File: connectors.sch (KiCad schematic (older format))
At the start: 3 parts, among them P1 CONN_02X04, P3 CONN_02X04

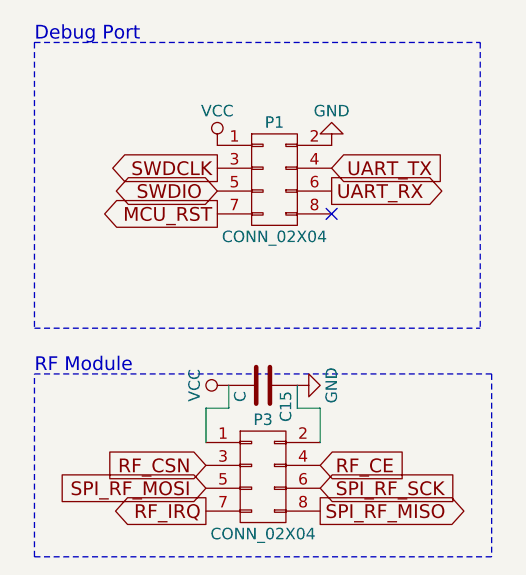
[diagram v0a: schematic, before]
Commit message: Fix Boot0 pin and add prices per component
Signed-off-by: Philip Luyckx <philip.luyckx@gmail.com>
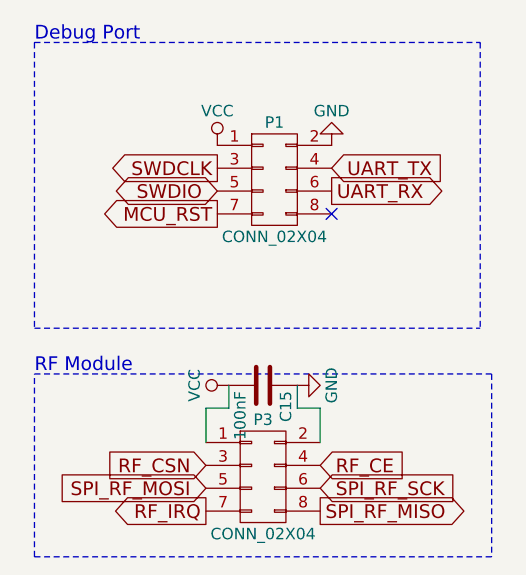
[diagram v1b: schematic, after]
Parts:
- C15: value C -> 100nF; Price (none) -> 0.02
- P1: Price (none) -> 0.13
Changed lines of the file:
@@
 F 2 "Socket_Strips:Socket_Strip_Straight_2x04" H 3150 2850 50  0001 C CNN
 F 3 "" H 3150 2850 50  0000 C CNN
+F 4 "0.13" H 3150 4050 60  0001 C CNN "Price"
 	1    3150 4050
 	1    0    0    -1
@@
 P 3100 4950
 F 0 "C15" H 3125 5050 50  0000 L CNN
-F 1 "C" H 3125 4850 50  0000 L CNN
+F 1 "100nF" H 3125 4850 50  0000 L CNN
 F 2 "Resistors_SMD:R_0805" H 3138 4800 50  0001 C CNN
 F 3 "" H 3100 4950 50  0000 C CNN
+F 4 "0.02" H 3100 4950 60  0001 C CNN "Price"
 	1    3100 4950
 	0    1    1    0

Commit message: Update schematics for V3:
 * Change DHT22 to HTU21D
 * Change schematic for MCP6044
 * Correct unused opamp + power supply
 * Reassign some cpu pins (for HTU21D)
 * Add LDO power supply for 1.8V
 * Update STM32CubeMx project
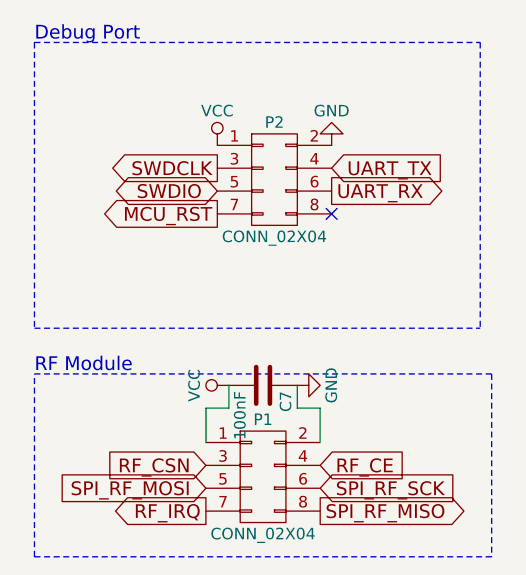
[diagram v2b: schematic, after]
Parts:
- renumbered C15 to C7, P3 to P1, P1 to P2
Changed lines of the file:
@@
 LIBS:CustomModules
 LIBS:CustomPower
-LIBS:CustomPowerConvertors
 LIBS:CustomTransistors
 LIBS:Custom_ShiftRegisters
@@
 LIBS:Relais
 LIBS:CustomDevices
+LIBS:CustomPowerConvertors
 LIBS:Sensor-cache
 EELAYER 25 0
@@
 $EndDescr
 $Comp
-L VCC #PWR012
+L VCC #PWR14
 U 1 1 565F5F2C
 P 2900 3900
-F 0 "#PWR012" H 2900 3750 50  0001 C CNN
+F 0 "#PWR14" H 2900 3750 50  0001 C CNN
 F 1 "VCC" H 2900 4050 50  0000 C CNN
 F 2 "" H 2900 3900 60  0000 C CNN
@@
 UART_TX
 $Comp
-L CONN_02X04 P3
+L CONN_02X04 P1
 U 1 1 56622904
 P 3100 5350
-F 0 "P3" H 3100 5600 50  0000 C CNN
+F 0 "P1" H 3100 5600 50  0000 C CNN
 F 1 "CONN_02X04" H 3100 5100 50  0000 C CNN
 F 2 "Socket_Strips:Socket_Strip_Straight_2x04" H 3100 4150 60  0001 C CNN
@@
 $EndComp
 $Comp
-L VCC #PWR013
+L VCC #PWR15
 U 1 1 56622A6F
 P 2950 4950
-F 0 "#PWR013" H 2950 4800 50  0001 C CNN
+F 0 "#PWR15" H 2950 4800 50  0001 C CNN
 F 1 "VCC" H 2950 5100 50  0000 C CNN
 F 2 "" H 2950 4950 60  0000 C CNN
@@
 $EndComp
 $Comp
-L GND #PWR014
+L GND #PWR16
 U 1 1 56622A8F
 P 3250 4950
-F 0 "#PWR014" H 3250 4700 50  0001 C CNN
+F 0 "#PWR16" H 3250 4700 50  0001 C CNN
 F 1 "GND" H 3250 4800 50  0000 C CNN
 F 2 "" H 3250 4950 60  0000 C CNN
@@
 	2100 4700 4050 4700
 $Comp
-L GND #PWR015
+L GND #PWR17
 U 1 1 5669F0F1
 P 3400 3900
-F 0 "#PWR015" H 3400 3650 50  0001 C CNN
+F 0 "#PWR17" H 3400 3650 50  0001 C CNN
 F 1 "GND" H 3400 3750 50  0000 C CNN
 F 2 "" H 3400 3900 60  0000 C CNN
@@
 	2100 3450 2100 4700
 $Comp
-L CONN_02X04 P1
+L CONN_02X04 P2
 U 1 1 56DBFF1C
 P 3150 4050
-F 0 "P1" H 3150 4300 50  0000 C CNN
+F 0 "P2" H 3150 4300 50  0000 C CNN
 F 1 "CONN_02X04" H 3150 3800 50  0000 C CNN
 F 2 "Socket_Strips:Socket_Strip_Straight_2x04" H 3150 2850 50  0001 C CNN
@@
 $EndComp
 $Comp
-L C C15
+L C C7
 U 1 1 56DC195B
 P 3100 4950
-F 0 "C15" H 3125 5050 50  0000 L CNN
+F 0 "C7" H 3125 5050 50  0000 L CNN
 F 1 "100nF" H 3125 4850 50  0000 L CNN
 F 2 "Resistors_SMD:R_0805" H 3138 4800 50  0001 C CNN

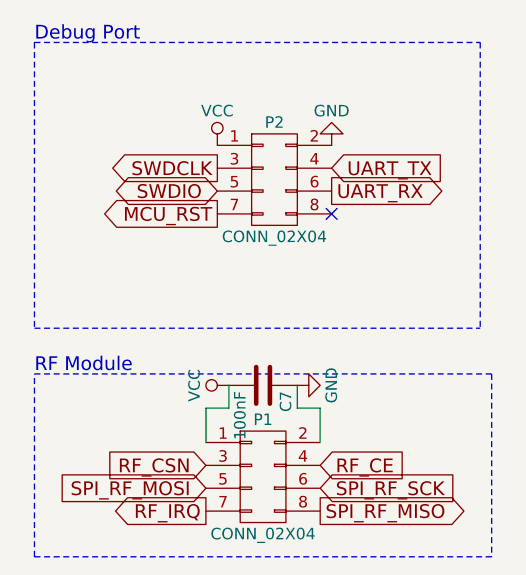
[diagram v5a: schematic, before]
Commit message: Update connectors to custom ones
Signed-off-by: Philip Luyckx <philip.luyckx@gmail.com>
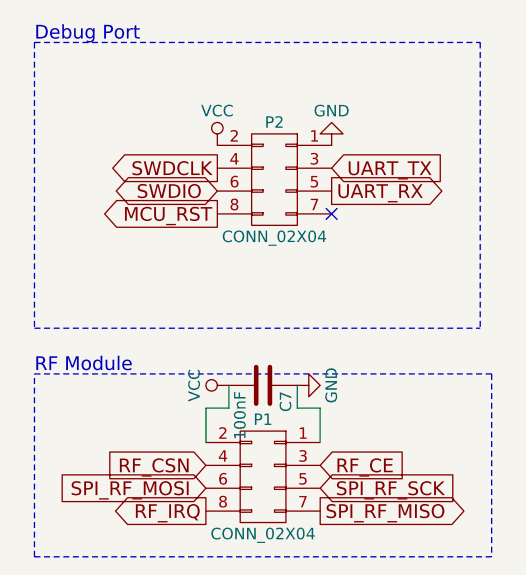
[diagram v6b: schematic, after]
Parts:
- P1: footprint Socket_Strips:Socket_Strip_Straight_2x04 -> PinHeaders:Pin_Header_Straight_2x04_SMD
- P2: footprint Socket_Strips:Socket_Strip_Straight_2x04 -> PinHeaders:Pin_Header_Straight_2x04_TH
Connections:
- net GND: now also P1.1 (P1), P2.1 (P1); no longer P1.2 (P2), P2.2 (P2)
- net MCU_RST: now also P2.8 (P8); no longer P2.7 (P7)
- net RF_CE: now also P1.3 (P3); no longer P1.4 (P4)
- net RF_CSN: now also P1.4 (P4); no longer P1.3 (P3)
- net RF_IRQ: now also P1.8 (P8); no longer P1.7 (P7)
- net SPI_RF_MISO: now also P1.7 (P7); no longer P1.8 (P8)
- net SPI_RF_MOSI: now also P1.6 (P6); no longer P1.5 (P5)
- net SPI_RF_SCK: now also P1.5 (P5); no longer P1.6 (P6)
- net SWDCLK: now also P2.4 (P4); no longer P2.3 (P3)
- net SWDIO: now also P2.6 (P6); no longer P2.5 (P5)
- net UART_RX: now also P2.5 (P5); no longer P2.6 (P6)
- net UART_TX: now also P2.3 (P3); no longer P2.4 (P4)
- net VCC: now also P1.2 (P2), P2.2 (P2); no longer P1.1 (P1), P2.1 (P1)
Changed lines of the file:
@@
 $EndDescr
 $Comp
-L VCC #PWR16
+L VCC #PWR016
 U 1 1 565F5F2C
 P 2900 3900
-F 0 "#PWR16" H 2900 3750 50  0001 C CNN
+F 0 "#PWR016" H 2900 3750 50  0001 C CNN
 F 1 "VCC" H 2900 4050 50  0000 C CNN
 F 2 "" H 2900 3900 60  0000 C CNN
@@
 F 0 "P1" H 3100 5600 50  0000 C CNN
 F 1 "CONN_02X04" H 3100 5100 50  0000 C CNN
-F 2 "Socket_Strips:Socket_Strip_Straight_2x04" H 3100 4150 60  0001 C CNN
+F 2 "PinHeaders:Pin_Header_Straight_2x04_SMD" H 3100 4150 60  0001 C CNN
 F 3 "" H 3100 4150 60  0000 C CNN
 	1    3100 5350
-	1    0    0    -1
+	-1   0    0    -1
 $EndComp
 $Comp
-L VCC #PWR17
+L VCC #PWR017
 U 1 1 56622A6F
 P 2950 4950
-F 0 "#PWR17" H 2950 4800 50  0001 C CNN
+F 0 "#PWR017" H 2950 4800 50  0001 C CNN
 F 1 "VCC" H 2950 5100 50  0000 C CNN
 F 2 "" H 2950 4950 60  0000 C CNN
@@
 $EndComp
 $Comp
-L GND #PWR18
+L GND #PWR018
 U 1 1 56622A8F
 P 3250 4950
-F 0 "#PWR18" H 3250 4700 50  0001 C CNN
+F 0 "#PWR018" H 3250 4700 50  0001 C CNN
 F 1 "GND" H 3250 4800 50  0000 C CNN
 F 2 "" H 3250 4950 60  0000 C CNN
@@
 	2100 4700 4050 4700
 $Comp
-L GND #PWR19
+L GND #PWR019
 U 1 1 5669F0F1
 P 3400 3900
-F 0 "#PWR19" H 3400 3650 50  0001 C CNN
+F 0 "#PWR019" H 3400 3650 50  0001 C CNN
 F 1 "GND" H 3400 3750 50  0000 C CNN
 F 2 "" H 3400 3900 60  0000 C CNN
@@
 F 0 "P2" H 3150 4300 50  0000 C CNN
 F 1 "CONN_02X04" H 3150 3800 50  0000 C CNN
-F 2 "Socket_Strips:Socket_Strip_Straight_2x04" H 3150 2850 50  0001 C CNN
+F 2 "PinHeaders:Pin_Header_Straight_2x04_TH" H 3150 2850 50  0001 C CNN
 F 3 "" H 3150 2850 50  0000 C CNN
 F 4 "0.13" H 3150 4050 60  0001 C CNN "Price"
 	1    3150 4050
-	1    0    0    -1
+	-1   0    0    -1
 $EndComp
 $Comp

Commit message: Add prices
Signed-off-by: Philip Luyckx <philip.luyckx@gmail.com>
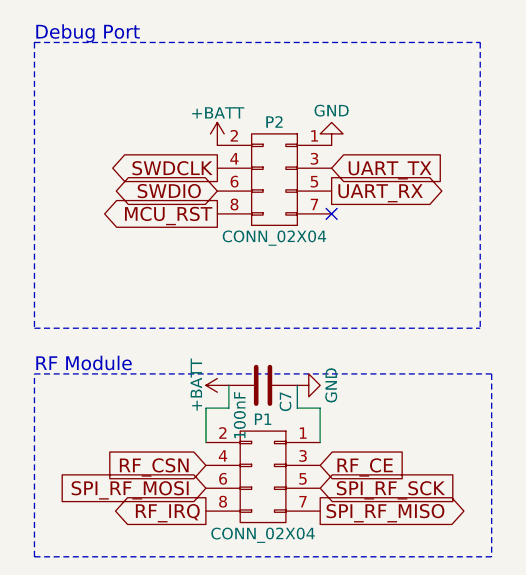
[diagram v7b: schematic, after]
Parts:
- P1: Price (none) -> 0.23
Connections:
- net VCC renamed +BATT
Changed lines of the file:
@@
 Comment4 ""
 $EndDescr
-$Comp
-L VCC #PWR016
-U 1 1 565F5F2C
-P 2900 3900
-F 0 "#PWR016" H 2900 3750 50  0001 C CNN
-F 1 "VCC" H 2900 4050 50  0000 C CNN
-F 2 "" H 2900 3900 60  0000 C CNN
-F 3 "" H 2900 3900 60  0000 C CNN
-	1    2900 3900
-	1    0    0    -1
-$EndComp
 Text GLabel 2900 4200 0    60   Output ~ 0
 MCU_RST
@@
 F 2 "PinHeaders:Pin_Header_Straight_2x04_SMD" H 3100 4150 60  0001 C CNN
 F 3 "" H 3100 4150 60  0000 C CNN
+F 4 "0.23" H 3100 5350 60  0001 C CNN "Price"
 	1    3100 5350
 	-1   0    0    -1
 $EndComp
 $Comp
-L VCC #PWR017
-U 1 1 56622A6F
-P 2950 4950
-F 0 "#PWR017" H 2950 4800 50  0001 C CNN
-F 1 "VCC" H 2950 5100 50  0000 C CNN
-F 2 "" H 2950 4950 60  0000 C CNN
-F 3 "" H 2950 4950 60  0000 C CNN
-	1    2950 4950
-	0    -1   -1   0
-$EndComp
-$Comp
-L GND #PWR018
+L GND #PWR016
 U 1 1 56622A8F
 P 3250 4950
-F 0 "#PWR018" H 3250 4700 50  0001 C CNN
+F 0 "#PWR016" H 3250 4700 50  0001 C CNN
 F 1 "GND" H 3250 4800 50  0000 C CNN
 F 2 "" H 3250 4950 60  0000 C CNN
@@
 	2100 4700 4050 4700
 $Comp
-L GND #PWR019
+L GND #PWR017
 U 1 1 5669F0F1
 P 3400 3900
-F 0 "#PWR019" H 3400 3650 50  0001 C CNN
+F 0 "#PWR017" H 3400 3650 50  0001 C CNN
 F 1 "GND" H 3400 3750 50  0000 C CNN
 F 2 "" H 3400 3900 60  0000 C CNN
@@
 Wire Wire Line
 	3250 5050 3250 4950
+$Comp
+L +BATT #PWR018
+U 1 1 58A78D35
+P 2900 3900
+F 0 "#PWR018" H 2900 3750 50  0001 C CNN
+F 1 "+BATT" H 2900 4040 50  0000 C CNN
+F 2 "" H 2900 3900 50  0000 C CNN
+F 3 "" H 2900 3900 50  0000 C CNN
+	1    2900 3900
+	1    0    0    -1
+$EndComp
+$Comp
+L +BATT #PWR019
+U 1 1 58A78D53
+P 2950 4950
+F 0 "#PWR019" H 2950 4800 50  0001 C CNN
+F 1 "+BATT" H 2950 5090 50  0000 C CNN
+F 2 "" H 2950 4950 50  0000 C CNN
+F 3 "" H 2950 4950 50  0000 C CNN
+	1    2950 4950
+	0    -1   -1   0
+$EndComp
 $EndSCHEMATC

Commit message: Finish layout
Signed-off-by: Philip Luyckx <philip.luyckx@gmail.com>
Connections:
- net +BATT: now also P2.1 (P1); no longer P2.2 (P2)
- net GND: now also P2.2 (P2); no longer P2.1 (P1)
- net MCU_RST: now also P2.7 (P7); no longer P2.8 (P8)
- net SWDCLK: now also P2.3 (P3); no longer P2.4 (P4)
- net SWDIO: now also P2.5 (P5); no longer P2.6 (P6)
- net UART_RX: now also P2.6 (P6); no longer P2.5 (P5)
- net UART_TX: now also P2.4 (P4); no longer P2.3 (P3)
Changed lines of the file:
@@
 F 4 "0.13" H 3150 4050 60  0001 C CNN "Price"
 	1    3150 4050
-	-1   0    0    -1
+	1    0    0    -1
 $EndComp
 $Comp
